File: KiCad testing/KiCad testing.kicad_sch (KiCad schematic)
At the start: 40 parts, among them J1 USB_A, Q1 IRF540N, Q2 IRF540N, Q3 IRF540N, Q4 IRF540N, U1 IR2213, U4 IR2213

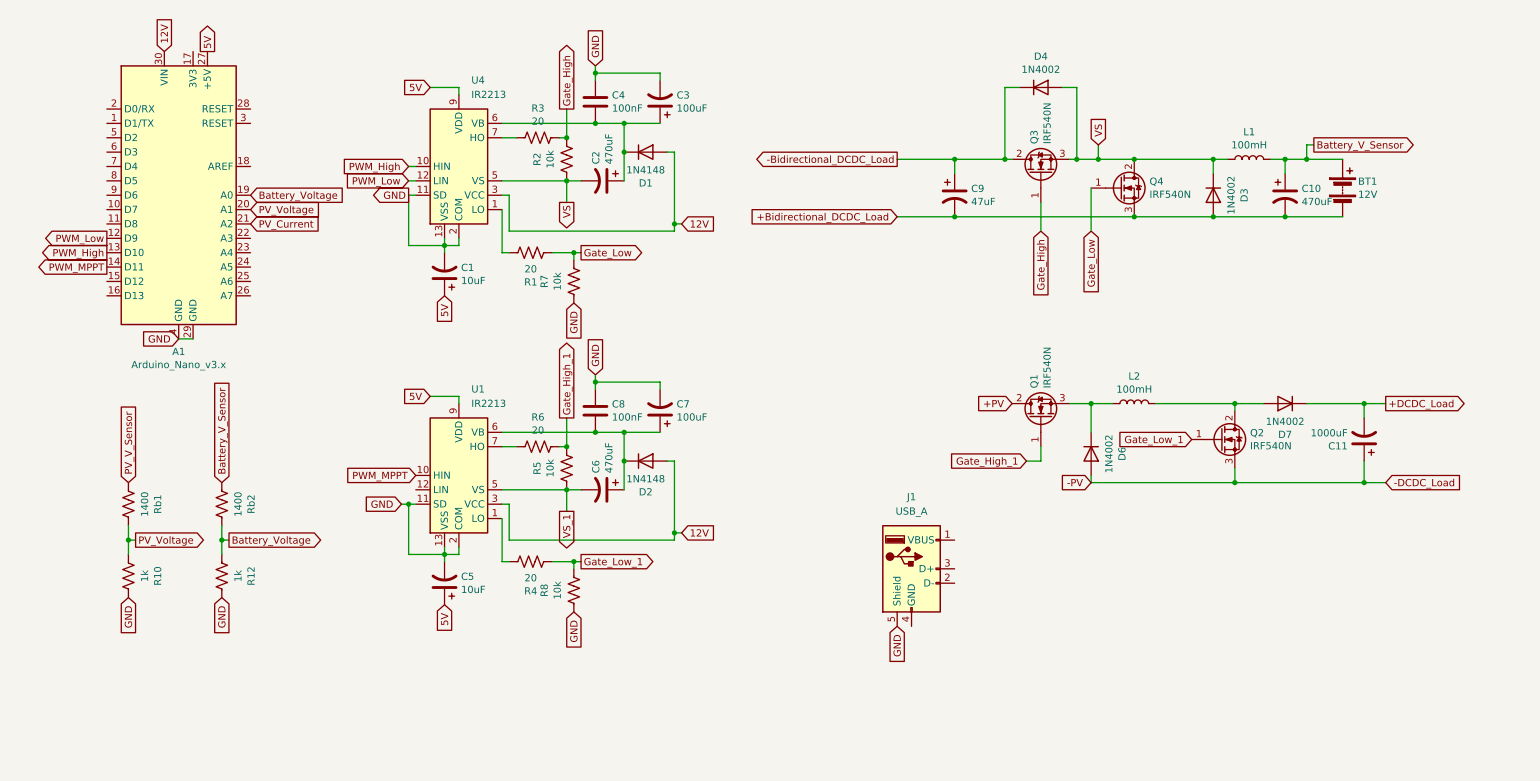
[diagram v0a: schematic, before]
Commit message: Schematic and PCB Redesign
Double checked all connections in the schematic.
1. Changed the Arduino Nano to an Arduino Uno Rev3
2. Changed the schematic for the two IR2113 nets so that they are more coherent.
3. Added and fixed certain things with the voltage and current sensors
4. Cleaned up the global labels.

Started redesigning the PCB to follow updated schematic and several other constraints.
1. Most power traces are now 1mm trace width to allow more power flow.
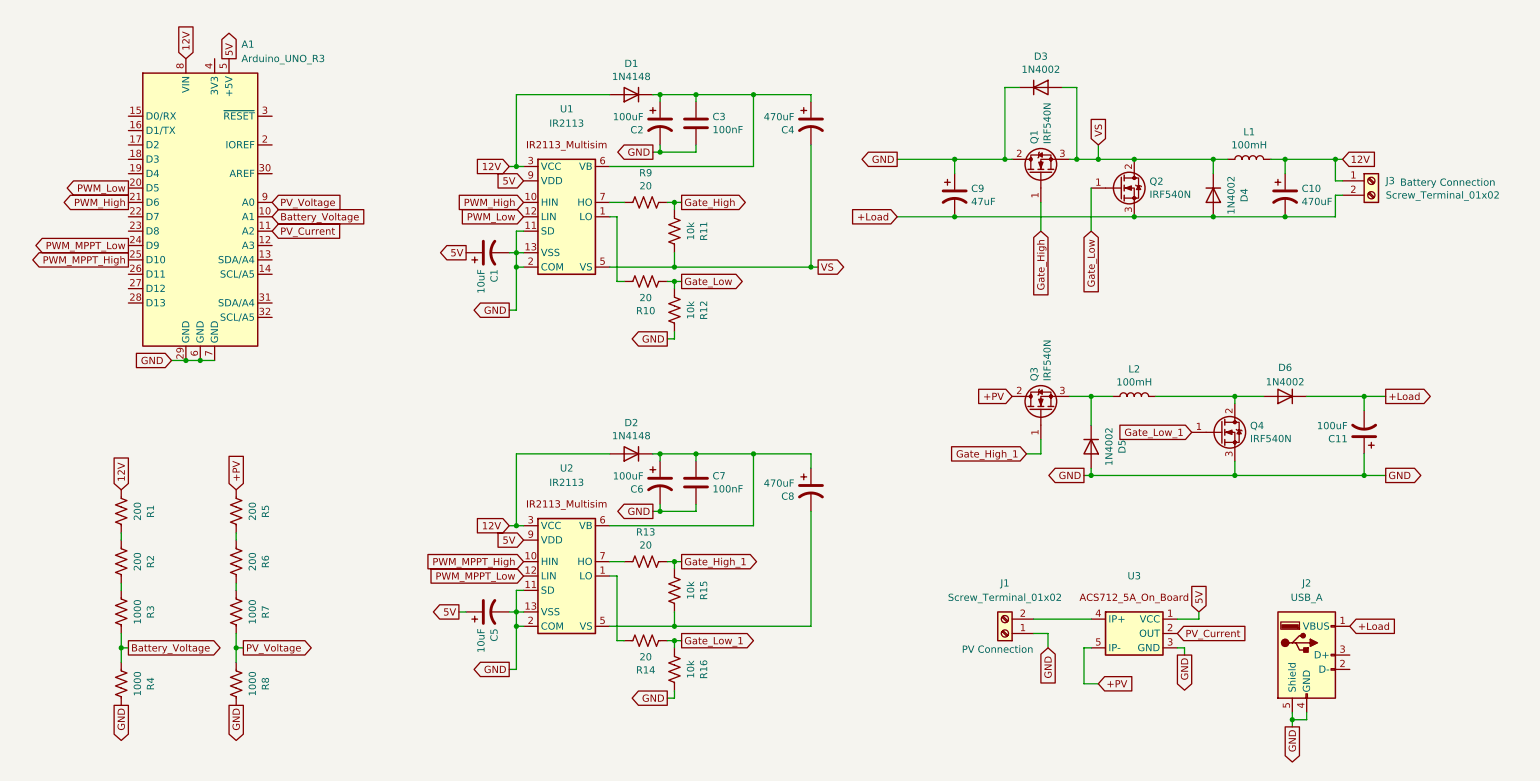
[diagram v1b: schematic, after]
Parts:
- removed A1: Arduino_Nano_v3.x, Module:Arduino_Nano, symbol KiCad testing-rescue:Arduino_Nano_v3.x-MCU_Module
- removed BT1: 12V, symbol Device:Battery
- removed C3: 100uF, Capacitor_THT:CP_Radial_D5.0mm_P2.00mm, symbol KiCad testing-rescue:CP1-Device
- removed C4: 100nF, Capacitor_THT:C_Disc_D4.7mm_W2.5mm_P5.00mm, symbol Device:C
- removed R3: 20, Resistor_THT:R_Axial_DIN0207_L6.3mm_D2.5mm_P10.16mm_Horizontal, symbol Device:R_US
- removed R7: 10k, Resistor_THT:R_Axial_DIN0207_L6.3mm_D2.5mm_P10.16mm_Horizontal, symbol Device:R_US
- removed U1, U4: IR2213, Package_DIP:DIP-14_W7.62mm, symbol Driver_FET:IR2213
- added A1: Arduino_UNO_R3, Module:Arduino_UNO_R3, symbol MCU_Module:Arduino_UNO_R3
- added C3: 100nF, Capacitor_THT:C_Disc_D4.7mm_W2.5mm_P5.00mm, symbol Device:C
- added C4: 470uF, Capacitor_THT:CP_Radial_D10.0mm_P5.00mm, symbol KiCad testing-rescue:CP1-Device
- added J1, J3: Screw_Terminal_01x02, TerminalBlock:TerminalBlock_Altech_AK300-2_P5.00mm, symbol Connector:Screw_Terminal_01x02
- added R10, R9: 20, Resistor_THT:R_Axial_DIN0207_L6.3mm_D2.5mm_P10.16mm_Horizontal, symbol Device:R_US
- added R11, R12: 10k, Resistor_THT:R_Axial_DIN0207_L6.3mm_D2.5mm_P10.16mm_Horizontal, symbol Device:R_US
- added R5, R6: 200, Resistor_THT:R_Axial_DIN0207_L6.3mm_D2.5mm_P10.16mm_Horizontal, symbol Device:R_US
- added U1, U2: IR2113, Package_DIP:DIP-14_W7.62mm, symbol New_Library:IR2113_Multisim
- added U3: ~, symbol New_Library:ACS712_5A_On_Board
- C11: value 1000uF -> 100uF
- C2: value 470uF -> 100uF; footprint Capacitor_THT:CP_Radial_D10.0mm_P5.00mm -> Capacitor_THT:CP_Radial_D5.0mm_P2.00mm
- R1: value 20 -> 200
- R2: value 10k -> 200
- R3: renamed from Rb1; value 1400 -> 1000; footprint (none) -> Resistor_THT:R_Axial_DIN0207_L6.3mm_D2.5mm_P10.16mm_Horizontal
- R4: renamed from R10; value 1k -> 1000
- R7: renamed from Rb2; value 1400 -> 1000; footprint (none) -> Resistor_THT:R_Axial_DIN0207_L6.3mm_D2.5mm_P10.16mm_Horizontal
- R8: renamed from R12; value 1k -> 1000
- renumbered C7 to C6, C8 to C7, C6 to C8, D4 to D3, D3 to D4, D6 to D5, D7 to D6, J1 to J2, Q3 to Q1, Q4 to Q2, Q1 to Q3, Q2 to Q4, R4 to R13, R6 to R14, R8 to R15, R5 to R16
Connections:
- net +Bidirectional_DCDC_Load is gone; now on net +Load: C10.2, C9.2, D4.2 (A), Q2.3 (S)
- net +DCDC_Load is gone; now on net +Load: C11.2, D6.1 (K)
- net -Bidirectional_DCDC_Load is gone; now on net GND: C9.1, D3.1 (K), Q1.2 (D)
- net -DCDC_Load is gone; now on net GND: C11.1, D5.2 (A), Q4.3 (S)
- net +PV: now also R5.1, U3.5 (IP-)
- net 12V: now also C10.1, L1.2, R1.1, A1.8 (VIN), J3.1 (Pin_1), U1.3 (VCC), U2.3 (VCC)
- net 5V: now also A1.5 (+5V), U1.9 (VDD), U2.9 (VDD), U3.1 (VCC)
- net Battery_Voltage: now also R3.2, R4.1, A1.10 (A1); no longer R7.2, R8.1
- net GND: now also C2.2, C7.2, J2.4 (GND), R16.2, A1.29 (GND), A1.6 (GND), A1.7 (GND), C3.2, J1.1 (Pin_1), R12.2, U1.11 (SD), U1.13 (VSS), U1.2 (COM), U2.11 (SD), U2.13 (VSS), U2.2 (COM), U3.3 (GND); no longer C7.1, R15.1
- net Gate_High: now also R11.1, R9.2; no longer R2.2
- net Gate_High_1: now also R13.2, R15.1; no longer R14.2, R16.2
- net Gate_Low: now also R10.1, R12.1; no longer R1.1
- net Gate_Low_1: now also R14.1, R16.1; no longer R13.1, R15.2
- net PV_Current: now also A1.11 (A2), U3.2 (OUT)
- net PV_Voltage: now also R7.2, R8.1, A1.9 (A0); no longer R3.2, R4.1
- net PWM_High: now also A1.21 (D6), U1.10 (HIN)
- net PWM_Low: now also A1.20 (D5), U1.12 (LIN)
- net VS: now also C4.2, R11.2, U1.5 (VS); no longer C2.2, R2.1
- net at C2.1, D1.1 (K): now also C3.1, C4.1, U1.6 (VB)
- net at R1.2: now also R2.1
- net at C6.1, C8.1, D2.1 (K): now also C7.1, U2.6 (VB); no longer C7.2
- net +Load: now reaches J2.1 (VBUS)
- net +Load: now also J3.2 (Pin_2)
- removed net Battery_V_Sensor: C10.1, L1.2, R7.1
- net PV_V_Sensor: no longer names the net of R3.1
- net PV_V_Sensor: now also R2.2
- net VS_1: no longer names the net of C8.2
- net VS_1: now also R15.2, U2.5 (VS); no longer R16.1
- new net: R14.2, U2.1 (LO)
- new net: R13.1, U2.7 (HO)
- new net: R10.2, U1.1 (LO)
- new net: R9.1, U1.7 (HO)
- new net: J1.2 (Pin_2), U3.4 (IP+)
- new net: R6.2, R7.1
- new net: R5.2, R6.1
- new net PWM_MPPT_High: A1.25 (D10), U2.10 (HIN)
- new net PWM_MPPT_Low: A1.24 (D9), U2.12 (LIN)
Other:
- note added: "Battery Connection"
- note added: "PV Connection"
- moved on the sheet: C11, C5, C6, C7, C8, D2, D5, D6, J2, L2, Q3, Q4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
